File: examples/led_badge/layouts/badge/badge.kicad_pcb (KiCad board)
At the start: 4 copper layers, 56.3 x 39 mm, 242 parts

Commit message: shipped badge board
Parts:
- LOGO1: footprint atopile_Logo_8x8mm:atopile_Logo_8x8mm -> atopile_Logo_25x6mm:atopile_Logo_25x6mm
- R12: footprint UNI_ROYAL_0402WGF1802TCE:R0402 -> YAGEO_RC0402FR_0718KL:R0402
- moved LOGO1 14.2 mm to (105.4, 83.2)
- moved B1 5.00 mm to (94.6, 104.2)
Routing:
- net power_3v3: track 177.6 -> 179.6 mm
- added copper zone on In1.Cu, net gnd

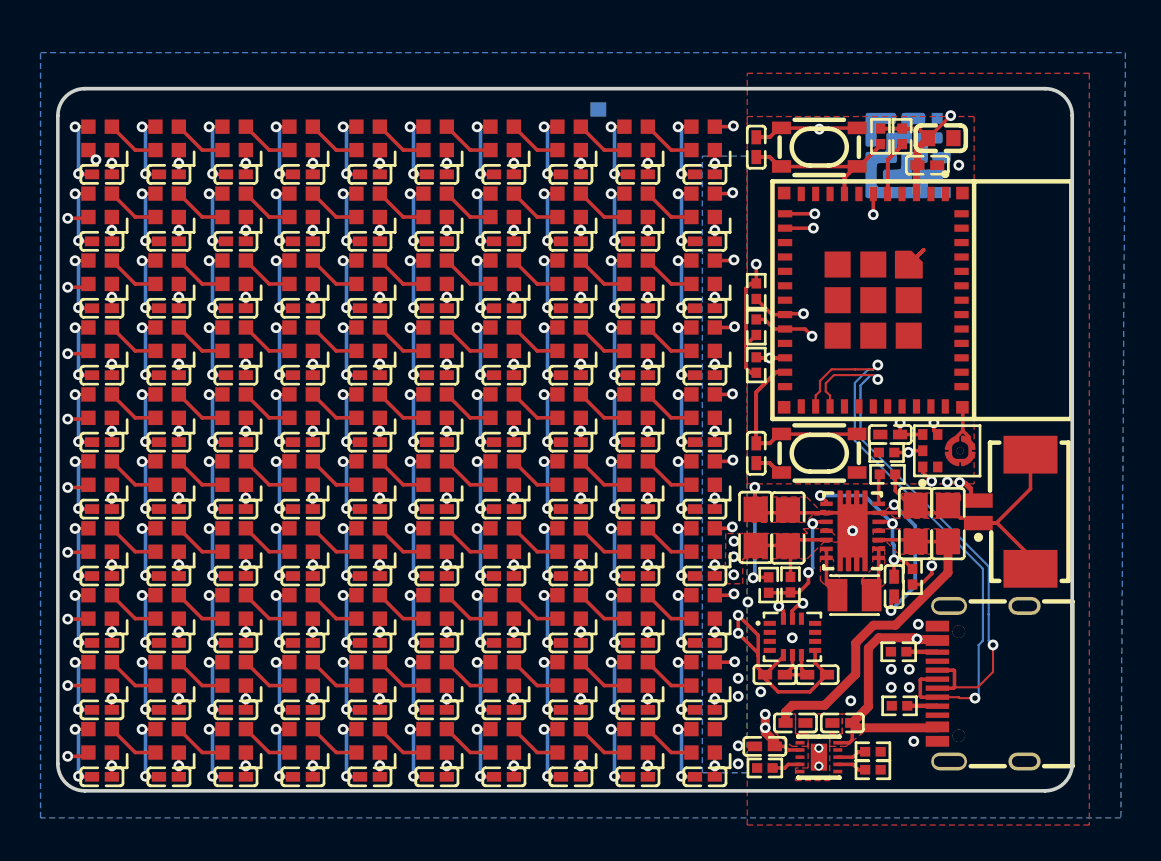
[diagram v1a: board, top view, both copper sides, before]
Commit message: Update regulator and fix layout
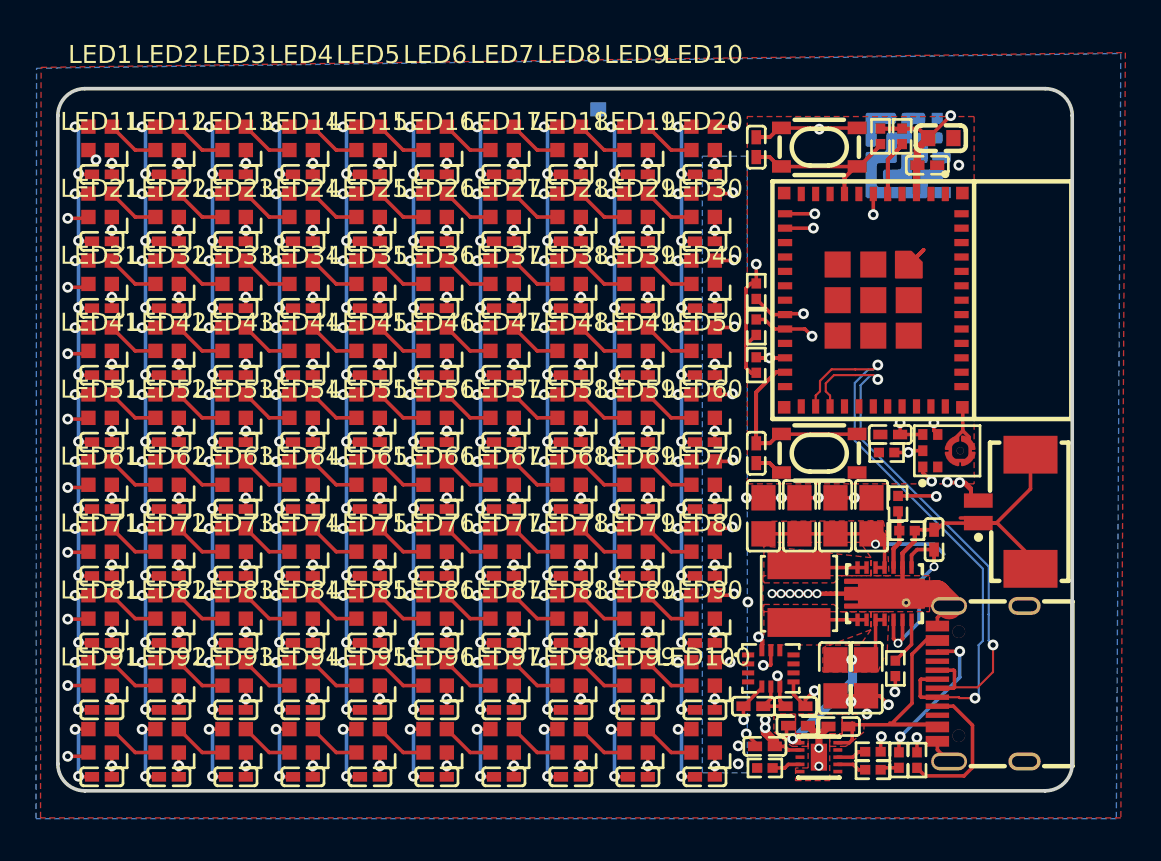
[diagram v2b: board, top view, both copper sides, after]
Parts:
- removed R6: 10kΩ ±1% 62.5mW, UNI_ROYAL_0402WGF1002TCE:R0402
- added C116: 22µF ±20% 6.3V X5R, Samsung_Electro_Mechanics_CL21A226MQQNNNE:C0805, F.Cu at (107.7, 103.2)
- added C117: 100nF ±10% 16V X7R, Samsung_Electro_Mechanics_CL05B104KO5NNNC:C0402, F.Cu at (117.1, 104.5)
- C110, C111: value 10µF ±10% 25V X5R -> 22µF ±20% 6.3V X5R; footprint Samsung_Electro_Mechanics_CL21A106KAYNNNE:C0805 -> Samsung_Electro_Mechanics_CL21A226MQQNNNE:C0805
- C112: value 100nF ±10% 16V X7R -> 22µF ±20% 6.3V X5R; footprint Samsung_Electro_Mechanics_CL05B104KO5NNNC:C0402 -> Samsung_Electro_Mechanics_CL21A226MQQNNNE:C0805
- C114: footprint Murata_Electronics_GRM155R60J106ME44D:C0402 -> Samsung_Electro_Mechanics_CL05A106MQ5NUNC:C0402
- C3, C4: value 10µF ±10% 25V X5R -> 10µF ±10% 16V X5R; footprint Samsung_Electro_Mechanics_CL21A106KAYNNNE:C0805 -> Samsung_Electro_Mechanics_CL21A106KOQNNNE:C0805
- L1: value (none) -> 1µH ±20% 6.7A 23mΩ; footprint Sunlord_WPN252012H1R5MT:IND-SMD_L2.5-W2.0_WPN252012H -> cjiang_FHD4020S_1R0MT:IND-SMD_L4.0-W4.0
- R1: value 10kΩ ±1% 62.5mW -> 150kΩ ±1% 62.5mW; footprint UNI_ROYAL_0402WGF1002TCE:R0402 -> UNI_ROYAL_0402WGF1503TCE:R0402
- R12: footprint YAGEO_RC0402FR_0718KL:R0402 -> UNI_ROYAL_0402WGF1802TCE:R0402
- R2: value 56kΩ ±1% 62.5mW -> 750kΩ ±1% 62.5mW; footprint UNI_ROYAL_0402WGF5602TCE:R0402 -> YAGEO_RC0402FR_07750KL:R0402
- U2: footprint TI_TPS63020DSJR:VSON-14_L4.0-W3.0-P0.50-BL-EP_TI_DSJ -> Texas_Instruments_TPS63020DSJR:VSON-14_L4.0-W3.0-P0.50-BL-EP_TI_DSJ
- moved R3 10.8 mm to (115.0, 111.7), turned to -90 degrees
- moved C3 9.70 mm to (113.3, 112.2), turned to -90 degrees
- moved C4 9.66 mm to (111.7, 112.2), turned to -90 degrees
- moved R1 8.26 mm to (115.6, 104.0), turned to 0 degrees
- moved R2 7.48 mm to (115.1, 102.5)
- moved C112 6.56 mm to (109.7, 103.2), turned to 90 degrees
- moved R10 6.01 mm to (115.2, 116.8), turned to -90 degrees
- moved C110 4.69 mm to (113.7, 103.2)
- moved C111 4.48 mm to (111.7, 103.2)
- moved U2 3.92 mm to (114.4, 107.5), turned to 180 degrees
- moved R9 3.17 mm to (116.2, 116.8), turned to 90 degrees
- moved L1 3.09 mm to (109.6, 107.5), turned to 90 degrees
- moved C2 2.12 mm to (107.1, 113.8)
- moved U1 2.12 mm to (108.1, 111.7)
- moved C1 2.12 mm to (109.4, 113.8)
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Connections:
- C112 pad 1: EN -> power_3v3
- R3 pad 2: gnd -> power_3v3
- U2 pad 13: gnd -> EN
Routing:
- net gnd: track 482.1 -> 493.7 mm, vias 219 -> 222
- net power_sys: track 19.5 -> 12.6 mm, vias 0 -> 2
- net B5: track 1.65 -> 8.30 mm, vias 0 -> 2
- net A5: track 1.60 -> 8.23 mm
- net usb_power: track 21.9 -> 15.6 mm, vias 2 -> 0
- net i2c_scl: track 21.4 -> 25.7 mm
- net FB: track 6.63 -> 3.28 mm, vias 2 -> 0
- net i2c_sda: track 23.0 -> 25.4 mm
- net power_3v3: track 179.6 -> 181.0 mm, vias 112 -> 110
- net L1: track 2.73 -> 3.81 mm
- net L2: track 2.82 -> 3.81 mm
- net PG: track 1.66 -> 2.64 mm
- net EN: track 10.3 -> 10.9 mm, vias 3 -> 2
- added copper zone on In2.Cu, net gnd
- added copper zone on In1.Cu, net power_3v3
- removed copper zone on B.Cu, net gnd
- removed copper zone on In1.Cu, net gnd
